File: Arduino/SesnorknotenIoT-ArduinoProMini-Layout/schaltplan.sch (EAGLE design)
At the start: 12 parts

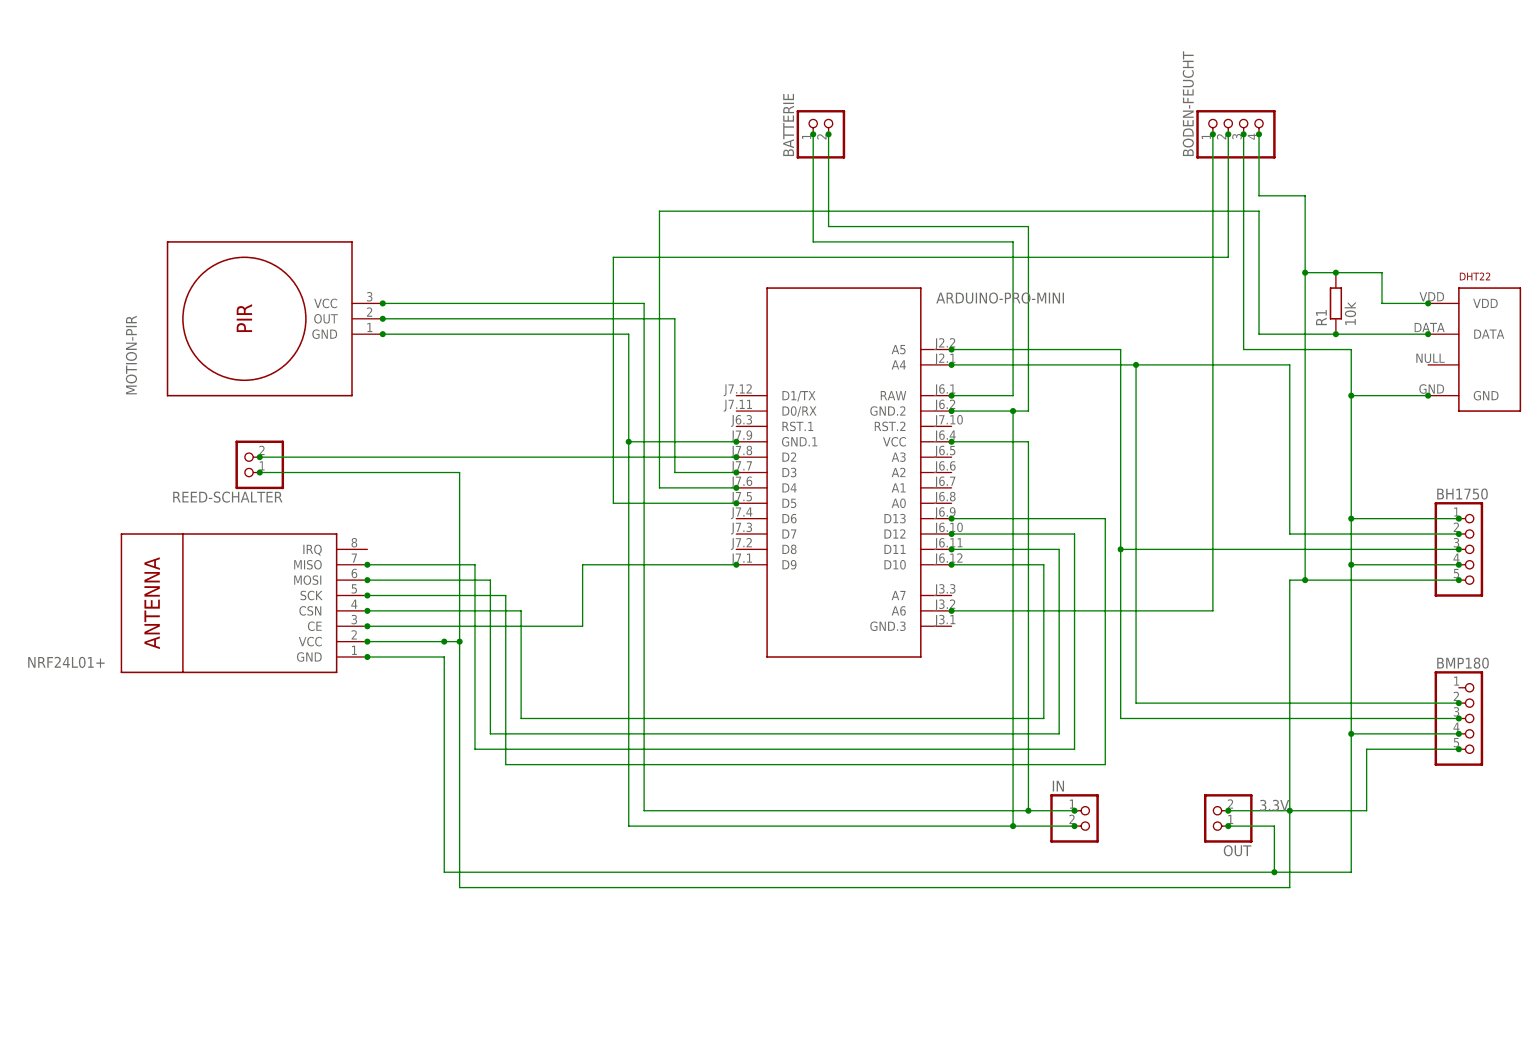
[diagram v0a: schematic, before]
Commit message: Änderungen Sender Verschlüsselung und Encodierung
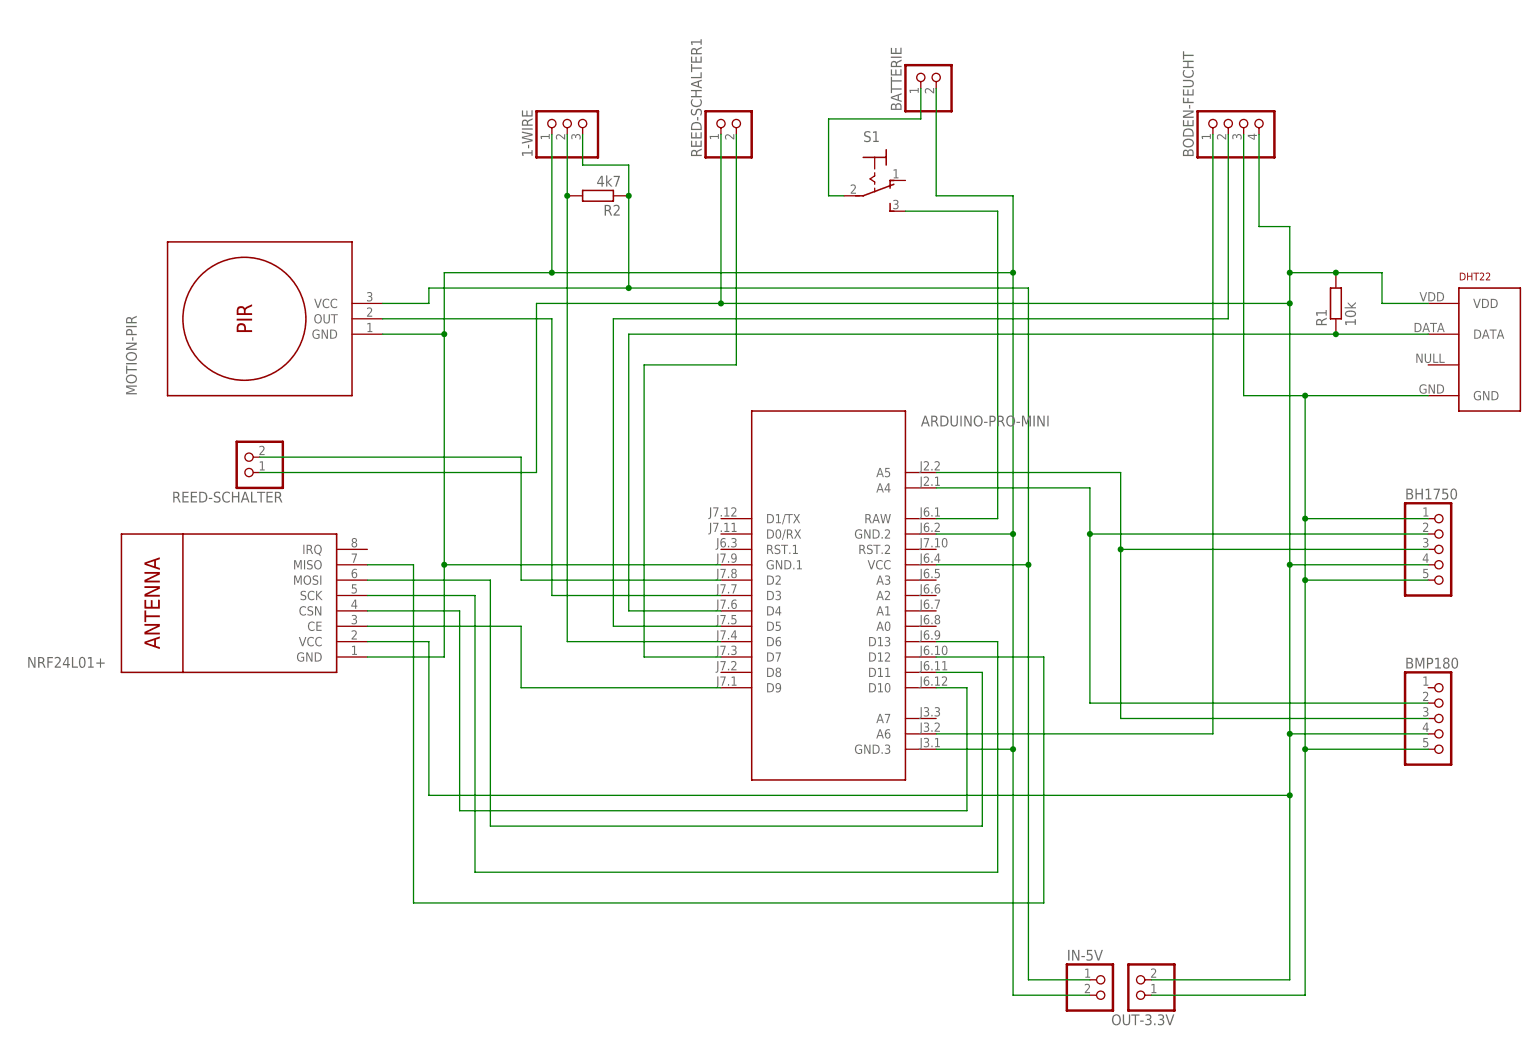
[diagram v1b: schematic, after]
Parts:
- removed IN, OUT: (no value), pinhead:PINHD-1X2
- added 1-WIRE: (no value), pinhead:PINHD-1X3
- added IN-5V, OUT-3.3V, REED-SCHALTER1: (no value), pinhead:PINHD-1X2
- added R2: 4k7, resistor:R-EU_0207/10
- added S1: (no value), switch:320-916
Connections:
- removed net RAW: ARDUINO-PRO-MINI.RAW, BATTERIE.1
- new net IN-3.3V: 1-WIRE.3, ARDUINO-PRO-MINI.VCC, IN-5V.1, MOTION-PIR.VCC, R2.1
- new net N$1: ARDUINO-PRO-MINI.RAW, S1.S
- new net N$7: 1-WIRE.2, ARDUINO-PRO-MINI.D6, R2.2
- new net N$9: ARDUINO-PRO-MINI.D7, REED-SCHALTER1.2
- net 3.3V: now also BH1750.4, BMP180.4, OUT-3.3V.2, REED-SCHALTER1.1; no longer BH1750.5, BMP180.5, OUT.2
- net GND: now also 1-WIRE.1, ARDUINO-PRO-MINI.GND.3, BH1750.5, BMP180.5, IN-5V.2, OUT-3.3V.1; no longer BH1750.4, BMP180.4, IN.2, OUT.1
- net N$2: now also BATTERIE.1, S1.P; no longer ARDUINO-PRO-MINI.VCC, IN.1, MOTION-PIR.VCC
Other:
- moved on the sheet: ARDUINO-PRO-MINI, BATTERIE, BH1750, BMP180

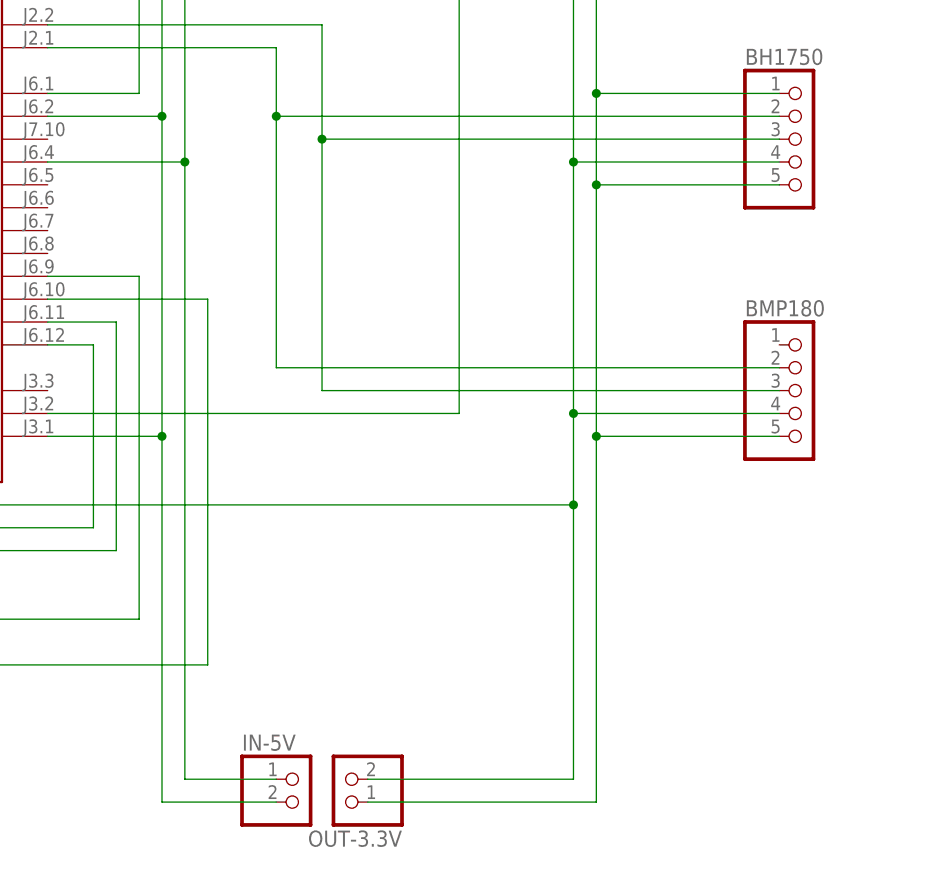
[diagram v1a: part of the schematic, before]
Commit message: Schaltplan für Arduino Pro Mini geändert Energiesparmodus aktivierbar
Signed-off-by: JanGerber <jan-456@t-online.de>
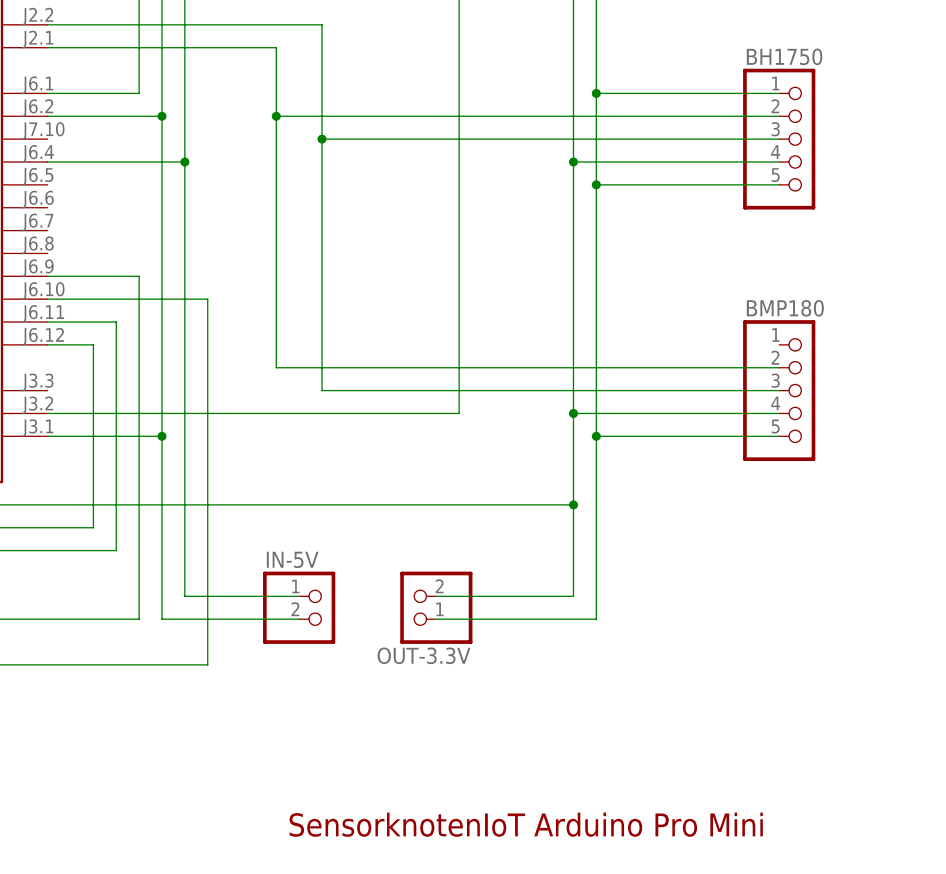
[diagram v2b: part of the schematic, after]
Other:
- note added: "SensorknotenIoT Arduino Pro Mini"
- moved on the sheet: IN-5V, OUT-3.3V
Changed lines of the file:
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@@
 <layer number="54" name="bGND_GNDA" color="7" fill="1" visible="no" active="no"/>
 <layer number="56" name="wert" color="7" fill="1" visible="no" active="no"/>
+<layer number="57" name="tCAD" color="7" fill="1" visible="no" active="no"/>
+<layer number="59" name="tCarbon" color="7" fill="1" visible="no" active="no"/>
+<layer number="60" name="bCarbon" color="7" fill="1" visible="no" active="no"/>
 <layer number="90" name="Modules" color="5" fill="1" visible="yes" active="yes"/>
 <layer number="91" name="Nets" color="2" fill="1" visible="yes" active="yes"/>
@@
 <layer number="108" name="tplace-old" color="7" fill="1" visible="yes" active="yes"/>
 <layer number="109" name="ref-old" color="7" fill="1" visible="yes" active="yes"/>
+<layer number="110" name="fp0" color="7" fill="1" visible="yes" active="yes"/>
+<layer number="111" name="LPC17xx" color="7" fill="1" visible="yes" active="yes"/>
+<layer number="112" name="tSilk" color="7" fill="1" visible="yes" active="yes"/>
+<layer number="113" name="IDFDebug" color="4" fill="1" visible="yes" active="yes"/>
 <layer number="116" name="Patch_BOT" color="7" fill="1" visible="yes" active="yes"/>
 <layer number="121" name="_tsilk" color="7" fill="1" visible="yes" active="yes"/>
 <layer number="122" name="_bsilk" color="7" fill="1" visible="yes" active="yes"/>
+<layer number="123" name="tTestmark" color="7" fill="1" visible="yes" active="yes"/>
+<layer number="124" name="bTestmark" color="7" fill="1" visible="yes" active="yes"/>
 <layer number="125" name="_tNames" color="7" fill="1" visible="yes" active="yes"/>
+<layer number="126" name="_bNames" color="7" fill="1" visible="yes" active="yes"/>
+<layer number="127" name="_tValues" color="7" fill="1" visible="yes" active="yes"/>
+<layer number="128" name="_bValues" color="7" fill="1" visible="yes" active="yes"/>
+<layer number="129" name="Mask" color="7" fill="1" visible="yes" active="yes"/>
+<layer number="131" name="tAdjust" color="7" fill="1" visible="yes" active="yes"/>
+<layer number="132" name="bAdjust" color="7" fill="1" visible="yes" active="yes"/>
 <layer number="144" name="Drill_legend" color="7" fill="1" visible="yes" active="yes"/>
+<layer number="150" name="Notes" color="7" fill="1" visible="yes" active="yes"/>
 <layer number="151" name="HeatSink" color="7" fill="1" visible="yes" active="yes"/>
+<layer number="152" name="_bDocu" color="7" fill="1" visible="yes" active="yes"/>
+<layer number="153" name="FabDoc1" color="7" fill="1" visible="yes" active="yes"/>
+<layer number="154" name="FabDoc2" color="7" fill="1" visible="yes" active="yes"/>
+<layer number="155" name="FabDoc3" color="7" fill="1" visible="yes" active="yes"/>
 <layer number="199" name="Contour" color="7" fill="1" visible="yes" active="yes"/>
 <layer number="200" name="200bmp" color="7" fill="1" visible="yes" active="yes"/>
@@
 <layer number="223" name="223bmp" color="7" fill="1" visible="yes" active="yes"/>
 <layer number="224" name="224bmp" color="7" fill="1" visible="yes" active="yes"/>
+<layer number="225" name="225bmp" color="7" fill="1" visible="yes" active="yes"/>
+<layer number="226" name="226bmp" color="7" fill="1" visible="yes" active="yes"/>
+<layer number="227" name="227bmp" color="7" fill="1" visible="yes" active="yes"/>
+<layer number="228" name="228bmp" color="7" fill="1" visible="yes" active="yes"/>
+<layer number="229" name="229bmp" color="7" fill="1" visible="yes" active="yes"/>
+<layer number="230" name="230bmp" color="7" fill="1" visible="yes" active="yes"/>
+<layer number="231" name="231bmp" color="7" fill="1" visible="yes" active="yes"/>
+<layer number="248" name="Housing" color="7" fill="1" visible="yes" active="yes"/>
+<layer number="249" name="Edge" color="7" fill="1" visible="yes" active="yes"/>
 <layer number="250" name="Descript" color="7" fill="1" visible="yes" active="yes"/>
 <layer number="251" name="SMDround" color="7" fill="1" visible="yes" active="yes"/>
 <layer number="254" name="cooling" color="7" fill="1" visible="yes" active="yes"/>
+<layer number="255" name="routoute" color="7" fill="1" visible="yes" active="yes"/>
 </layers>
 <schematic xreflabel="%F%N/%S.%C%R" xrefpart="/%S.%C%R">
 <attributes>
+<attribute name="CNAME" value="Studienarbeit 2016/2017"/>
+<attribute name="CREVISION" value="3.5"/>
+<attribute name="DESIGNER" value="Jan G. &amp; David P."/>
 </attributes>
 <variantdefs>
@@
 <part name="IN-5V" library="pinhead" deviceset="PINHD-1X2" device=""/>
 <part name="OUT-3.3V" library="pinhead" deviceset="PINHD-1X2" device=""/>
+<part name="FRAME1" library="SparkFun-Aesthetics" deviceset="FRAME-A4L" device=""/>
 </parts>
 <sheets>
 <sheet>
 <plain>
+<text x="107.95" y="-31.75" size="2.54" layer="94">SensorknotenIoT Arduino Pro Mini</text>
 </plain>
 <instances>
@@
 <instance part="REED-SCHALTER1" gate="G$1" x="48.26" y="116.84" rot="R90"/>
 <instance part="ARDUINO-PRO-MINI" gate="G$1" x="63.5" y="38.1"/>
-<instance part="IN-5V" gate="G$1" x="109.22" y="-27.94"/>
-<instance part="OUT-3.3V" gate="G$1" x="114.3" y="-25.4" rot="R180"/>
+<instance part="IN-5V" gate="G$1" x="111.76" y="-7.62"/>
+<instance part="OUT-3.3V" gate="G$1" x="121.92" y="-5.08" rot="R180"/>
+<instance part="FRAME1" gate="G$1" x="-73.66" y="-43.18" smashed="yes">
+<attribute name="LAST_DATE_TIME" x="107.95" y="-36.83" size="2.286" layer="94" font="vector"/>
+<attribute name="SHEET" x="121.92" y="-41.91" size="2.54" layer="94" font="vector"/>
+<attribute name="CNAME" x="107.95" y="-26.67" size="2.54" layer="94" font="vector"/>
+<attribute name="DESIGNER" x="152.6" y="-36.83" size="2.54" layer="94" font="vector"/>
+<attribute name="CREVISION" x="161.26" y="-42.01" size="2.54" layer="94" font="vector"/>
+</instance>
 </instances>
 <busses>
@@
 <pinref part="ARDUINO-PRO-MINI" gate="G$1" pin="VCC"/>
 <wire x1="81.28" y1="43.18" x2="96.52" y2="43.18" width="0.1524" layer="91"/>
-<wire x1="96.52" y1="43.18" x2="96.52" y2="-25.4" width="0.1524" layer="91"/>
+<wire x1="96.52" y1="43.18" x2="96.52" y2="-5.08" width="0.1524" layer="91"/>
 <pinref part="IN-5V" gate="G$1" pin="1"/>
-<wire x1="96.52" y1="-25.4" x2="106.68" y2="-25.4" width="0.1524" layer="91"/>
+<wire x1="96.52" y1="-5.08" x2="109.22" y2="-5.08" width="0.1524" layer="91"/>
 <wire x1="96.52" y1="43.18" x2="96.52" y2="88.9" width="0.1524" layer="91"/>
 <junction x="96.52" y="43.18"/>
@@
 <segment>
 <pinref part="OUT-3.3V" gate="G$1" pin="1"/>
-<wire x1="116.84" y1="-27.94" x2="142.24" y2="-27.94" width="0.1524" layer="91"/>
-<wire x1="142.24" y1="-27.94" x2="142.24" y2="12.7" width="0.1524" layer="91"/>
+<wire x1="124.46" y1="-7.62" x2="142.24" y2="-7.62" width="0.1524" layer="91"/>
+<wire x1="142.24" y1="-7.62" x2="142.24" y2="12.7" width="0.1524" layer="91"/>
 <pinref part="BMP180" gate="A" pin="5"/>
 <wire x1="142.24" y1="12.7" x2="162.56" y2="12.7" width="0.1524" layer="91"/>
@@
 <wire x1="93.98" y1="48.26" x2="81.28" y2="48.26" width="0.1524" layer="91"/>
 <pinref part="IN-5V" gate="G$1" pin="2"/>
-<wire x1="106.68" y1="-27.94" x2="93.98" y2="-27.94" width="0.1524" layer="91"/>
-<wire x1="93.98" y1="-27.94" x2="93.98" y2="12.7" width="0.1524" layer="91"/>
+<wire x1="109.22" y1="-7.62" x2="93.98" y2="-7.62" width="0.1524" layer="91"/>
+<wire x1="93.98" y1="-7.62" x2="93.98" y2="12.7" width="0.1524" layer="91"/>
 <junction x="93.98" y="48.26"/>
 <pinref part="ARDUINO-PRO-MINI" gate="G$1" pin="GND.3"/>
@@
 <wire x1="139.7" y1="15.24" x2="139.7" y2="5.08" width="0.1524" layer="91"/>
 <pinref part="OUT-3.3V" gate="G$1" pin="2"/>
-<wire x1="139.7" y1="5.08" x2="139.7" y2="-25.4" width="0.1524" layer="91"/>
-<wire x1="139.7" y1="-25.4" x2="116.84" y2="-25.4" width="0.1524" layer="91"/>
+<wire x1="139.7" y1="5.08" x2="139.7" y2="-5.08" width="0.1524" layer="91"/>
+<wire x1="139.7" y1="-5.08" x2="124.46" y2="-5.08" width="0.1524" layer="91"/>
 <pinref part="BH1750" gate="A" pin="4"/>
 <wire x1="162.56" y1="43.18" x2="139.7" y2="43.18" width="0.1524" layer="91"/>
